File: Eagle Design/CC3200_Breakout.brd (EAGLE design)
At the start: 160 x 100 mm, 49 parts, among them U15 AT25FS010, Y2 32.768KHz, Y3 407MHz

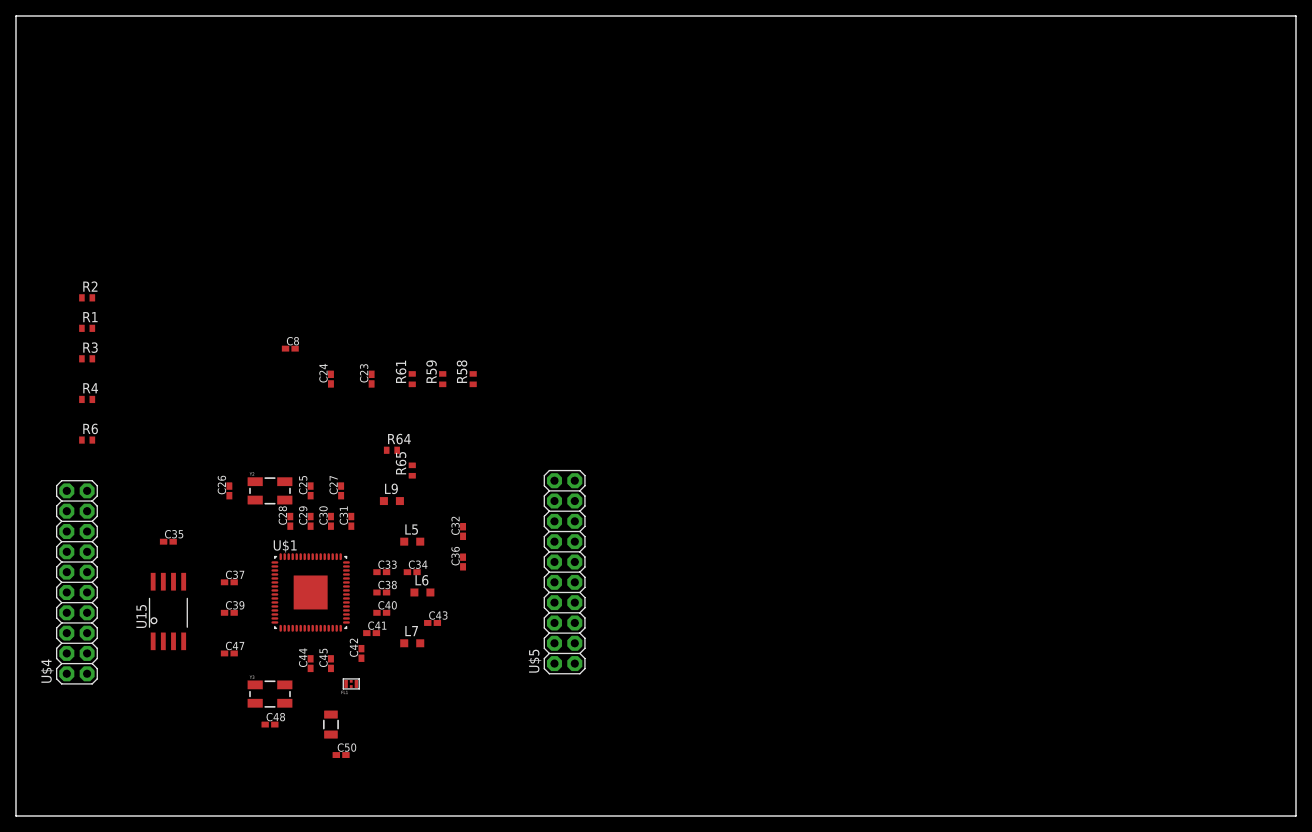
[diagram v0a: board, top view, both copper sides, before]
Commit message: Some placement and renaming
Removed Pull up and Pull down from Flash Chip and rename SPI pins
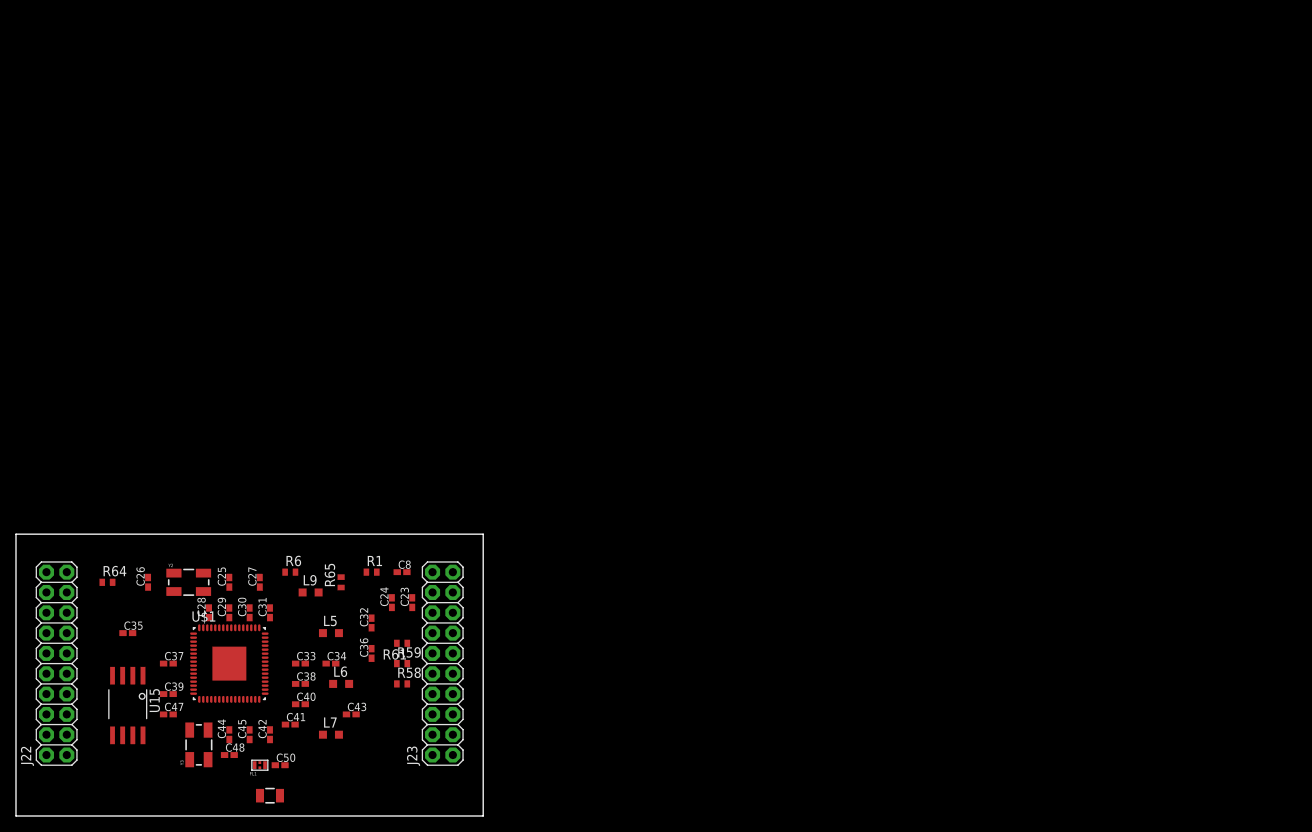
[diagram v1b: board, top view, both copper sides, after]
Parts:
- removed R2, R3, R4: 100k, resistor:R0402
- removed U$4, U$5: M10X2, SparkFun-Connectors:2X10
- added J22, J23: M10X2, SparkFun-Connectors:2X10
- moved R1 46.8 mm to (44.5, 30.5)
- moved R64 39.2 mm to (11.4, 29.2)
- moved R58 39.1 mm to (48.3, 16.5), turned to 0 degrees
- moved R59 35.9 mm to (48.3, 19.1), turned to 0 degrees
- moved R61 33.0 mm to (48.3, 21.6), turned to 180 degrees
- moved C8 31.2 mm to (48.3, 30.5)
- moved R6 30.3 mm to (34.3, 30.5)
- moved C24 29.0 mm to (47.0, 26.7)
- moved C23 28.4 mm to (49.5, 26.7)
- moved R65 16.6 mm to (40.6, 29.2)
- moved C32 16.2 mm to (44.5, 24.1)
- moved C36 16.2 mm to (44.5, 20.3)
- moved C34 15.3 mm to (39.4, 19.1)
- moved C41 15.3 mm to (34.3, 11.4)
- moved C43 15.3 mm to (41.9, 12.7)
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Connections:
- removed net 1: U$1.1, U$4.17
- removed net 2: U$1.2, U$4.19
- removed net 5: U$1.5, U$4.13
- removed net 6: U$1.6, U$5.14
- removed net 7: U$1.7, U$5.12
- removed net 8: U$1.8, U$5.6
- removed net N$15: U$4.1
- removed net N$77: U$4.2
- removed net N$78: U$4.4
- new net SCL: J22.17, U$1.1
- new net SDA: J22.19, U$1.2
- new net SPI_CLK: J22.13, U$1.5
- new net SPI_CS: J23.6, U$1.8
- new net SPI_MISO: J23.14, U$1.6
- new net SPI_MOSI: J23.12, U$1.7
- new net VCC_BRD: J22.1
- new net VCC_MCU_5V: J22.2
- net 15: now also J23.20; no longer U$5.20
- net 16: now also J23.17; no longer U$5.17
- net 17: now also J23.19; no longer U$5.19
- net 18: now also J23.4; no longer U$5.4
- net 21: now also J23.16; no longer U$5.16
- net 3: now also J22.7; no longer U$4.7
- net 4: now also J22.5; no longer U$4.5
- net 45: now also J23.8; no longer U$5.8
- net 50: now also J22.20; no longer U$4.20
- net 53: now also J22.16; no longer U$4.16
- net 55: now also J23.18; no longer U$5.18
- net 57: now also J22.6; no longer U$4.6
- net 58: now also J22.3; no longer U$4.3
- net 59: now also J22.11; no longer U$4.11
- net 60: now also J22.8; no longer U$4.8
- net 61: now also J22.9; no longer U$4.9
- net 62: now also J22.15; no longer U$4.15
- net 63: now also J22.14; no longer U$4.14
- net 64: now also J22.18; no longer U$4.18
- net GND: now also J22.4, J23.2; no longer R3.1, R4.1, U$5.2
- net N$30: no longer R2.2
- net N$32: no longer R4.2
- net N$33: no longer R3.2
- net N$47: now also J23.1; no longer U$5.1
- net N$48: now also J23.3; no longer U$5.3
- net N$49: now also J23.5; no longer U$5.5
- net N$50: now also J23.7; no longer U$5.7
- net N$51: now also J23.9; no longer U$5.9
- net N$52: now also J23.11; no longer U$5.11
- net N$53: now also J23.13; no longer U$5.13
- net N$54: now also J23.15; no longer U$5.15
- net N$81: now also J22.10; no longer U$4.10
- net N$82: now also J22.12; no longer U$4.12
- net N$91: now also J23.10; no longer U$5.10
- net V_BATT: no longer R2.1
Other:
- board size 160 x 100 mm -> 58.4 x 35.2 mm
